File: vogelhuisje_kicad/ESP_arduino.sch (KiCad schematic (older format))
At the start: 6 parts, among them J5 PMS5003

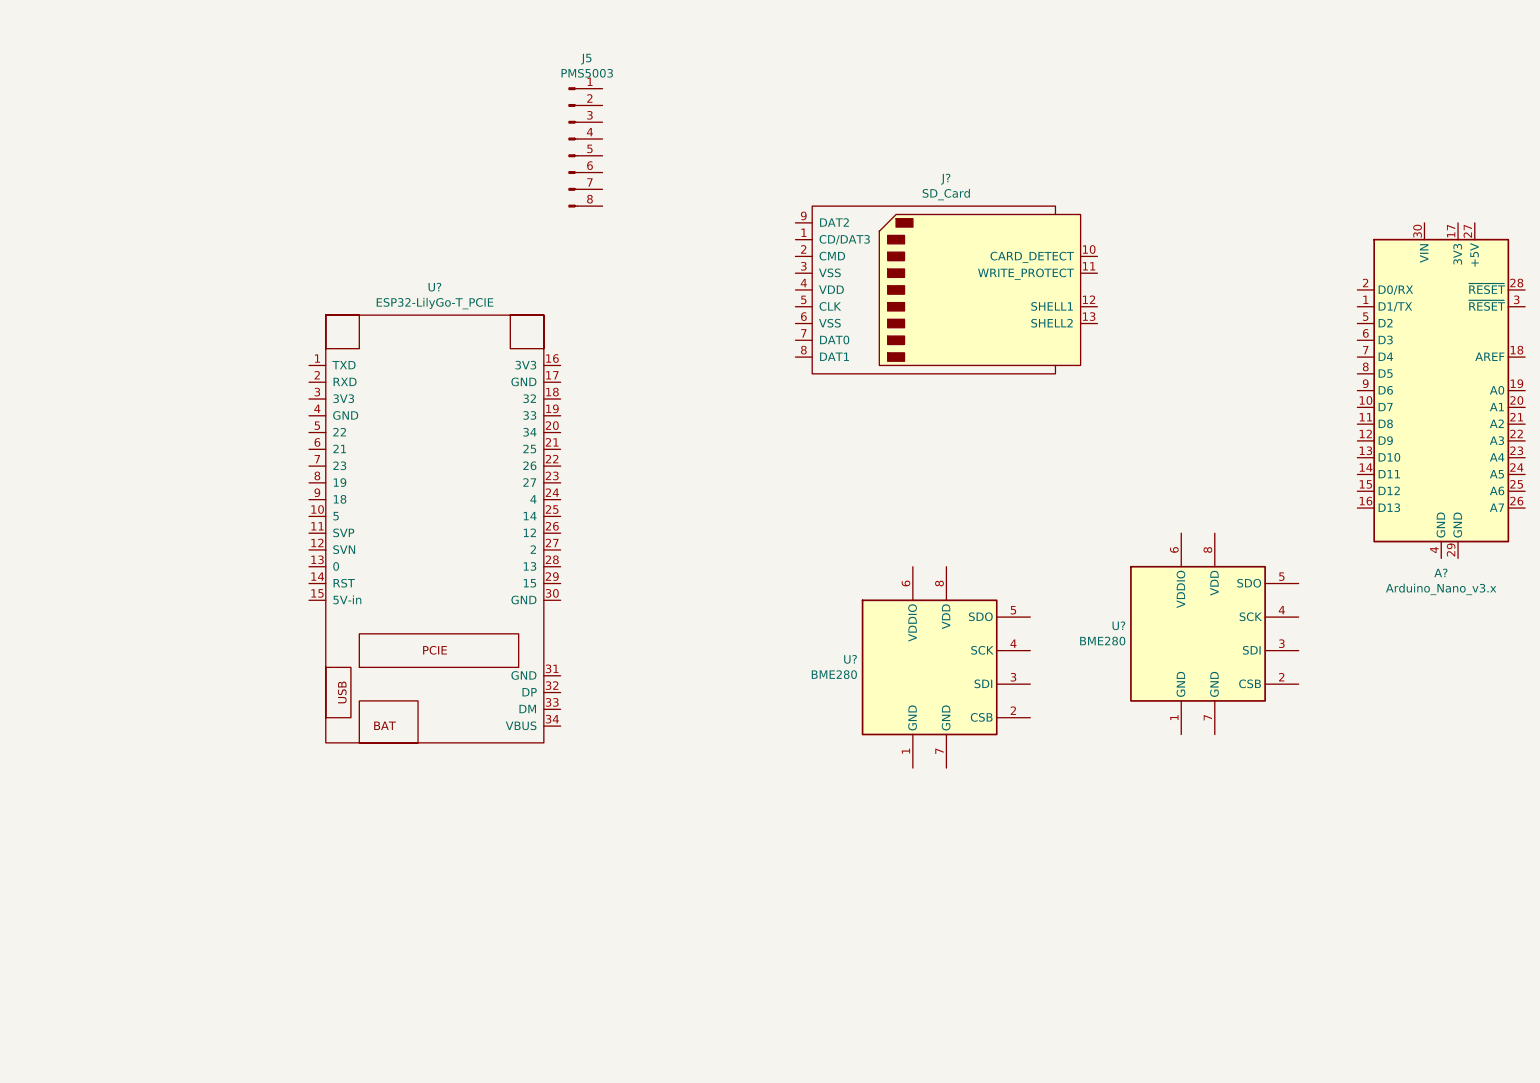
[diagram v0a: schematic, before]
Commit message: Add Camera to schematic
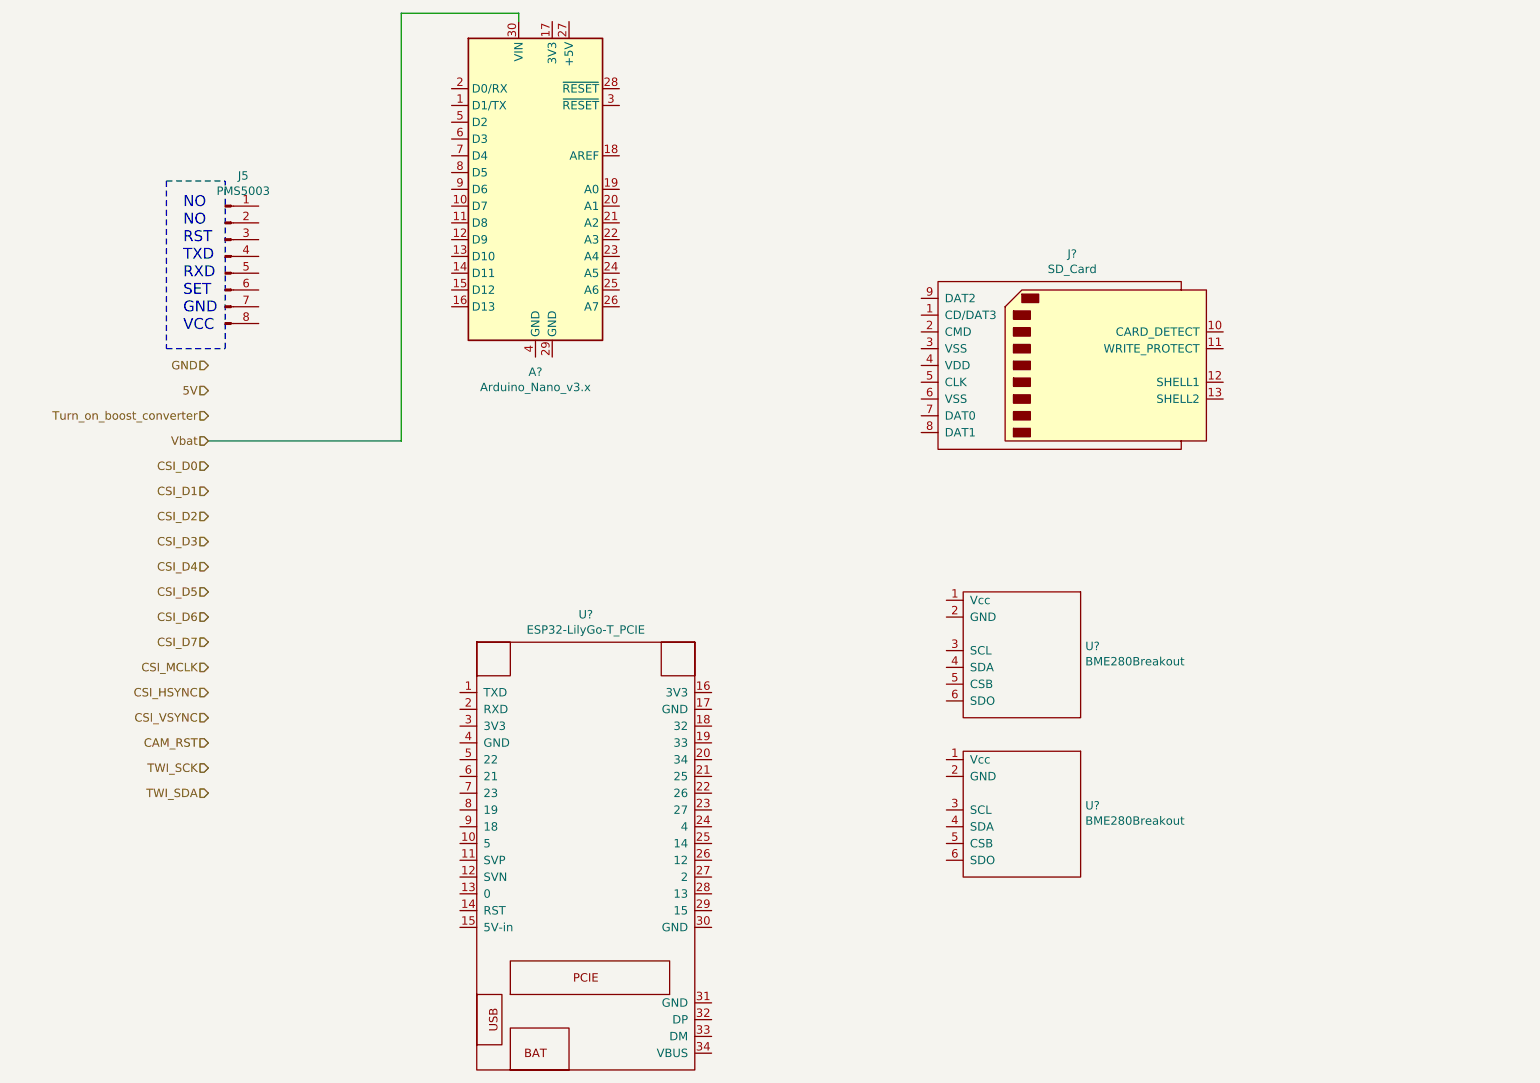
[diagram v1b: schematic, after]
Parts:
- removed U? (x2): BME280, Package_LGA:Bosch_LGA-8_2.5x2.5mm_P0.65mm_ClockwisePinNumbering, symbol Sensor:BME280
- added U? (x2): BME280Breakout, Components:Breakout-6, symbol voglehuisje_sensors_and_ESP:BME280Breakout
- J5: footprint (none) -> Components:PinHeader_1x08_P2.54mm_Vertical_G7
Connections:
- net Vbat: now reaches A?.30 (VIN)
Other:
- note added: "NO\nNO\nRST\nTXD\nRXD\nSET\nGND\nVCC"
- moved on the sheet: A?, J5, J?, U?
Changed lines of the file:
@@
 $Descr A4 11693 8268
 encoding utf-8
-Sheet 3 3
+Sheet 3 4
 Title ""
 Date ""
@@
 L MCU_Module:Arduino_Nano_v3.x A?
 U 1 1 6264AB53
-P 9350 2850
-F 0 "A?" H 9350 1761 50  0000 C CNN
-F 1 "Arduino_Nano_v3.x" H 9350 1670 50  0000 C CNN
-F 2 "Module:Arduino_Nano" H 9350 2850 50  0001 C CIN
-F 3 "http://www.mouser.com/pdfdocs/Gravitech_Arduino_Nano3_0.pdf" H 9350 2850 50  0001 C CNN
-	1    9350 2850
+P 3950 1650
+F 0 "A?" H 3950 561 50  0000 C CNN
+F 1 "Arduino_Nano_v3.x" H 3950 470 50  0000 C CNN
+F 2 "Module:Arduino_Nano" H 3950 1650 50  0001 C CIN
+F 3 "http://www.mouser.com/pdfdocs/Gravitech_Arduino_Nano3_0.pdf" H 3950 1650 50  0001 C CNN
+	1    3950 1650
 	1    0    0    -1
 $EndComp
@@
 L voglehuisje_sensors_and_ESP:ESP32-LilyGo-T_PCIE U?
 U 1 1 6264F9C2
-P 3300 4050
-F 0 "U?" H 3350 5865 50  0000 C CNN
-F 1 "ESP32-LilyGo-T_PCIE" H 3350 5774 50  0000 C CNN
-F 2 "Components:Tity-LilyGo" H 3250 4150 50  0001 C CNN
-F 3 "" H 3250 4150 50  0001 C CNN
-	1    3300 4050
+P 4200 6000
+F 0 "U?" H 4250 7815 50  0000 C CNN
+F 1 "ESP32-LilyGo-T_PCIE" H 4250 7724 50  0000 C CNN
+F 2 "Components:Tity-LilyGo" H 4150 6100 50  0001 C CNN
+F 3 "" H 4150 6100 50  0001 C CNN
+	1    4200 6000
 	1    0    0    -1
 $EndComp
@@
 L Connector:SD_Card J?
 U 1 1 62653AAF
-P 6400 2250
-F 0 "J?" H 6400 2915 50  0000 C CNN
-F 1 "SD_Card" H 6400 2824 50  0000 C CNN
-F 2 "" H 6400 2250 50  0001 C CNN
-F 3 "http://portal.fciconnect.com/Comergent//fci/drawing/10067847.pdf" H 6400 2250 50  0001 C CNN
-	1    6400 2250
-	1    0    0    -1
-$EndComp
-$Comp
-L Sensor:BME280 U?
-U 1 1 62653FC9
-P 6300 4500
-F 0 "U?" H 5871 4546 50  0000 R CNN
-F 1 "BME280" H 5871 4455 50  0000 R CNN
-F 2 "Package_LGA:Bosch_LGA-8_2.5x2.5mm_P0.65mm_ClockwisePinNumbering" H 7800 4050 50  0001 C CNN
-F 3 "https://ae-bst.resource.bosch.com/media/_tech/media/datasheets/BST-BME280-DS002.pdf" H 6300 4300 50  0001 C CNN
-	1    6300 4500
-	1    0    0    -1
-$EndComp
-$Comp
-L Sensor:BME280 U?
-U 1 1 626542C0
-P 7900 4300
-F 0 "U?" H 7471 4346 50  0000 R CNN
-F 1 "BME280" H 7471 4255 50  0000 R CNN
-F 2 "Package_LGA:Bosch_LGA-8_2.5x2.5mm_P0.65mm_ClockwisePinNumbering" H 9400 3850 50  0001 C CNN
-F 3 "https://ae-bst.resource.bosch.com/media/_tech/media/datasheets/BST-BME280-DS002.pdf" H 7900 4100 50  0001 C CNN
-	1    7900 4300
+P 7150 2700
+F 0 "J?" H 7150 3365 50  0000 C CNN
+F 1 "SD_Card" H 7150 3274 50  0000 C CNN
+F 2 "" H 7150 2700 50  0001 C CNN
+F 3 "http://portal.fciconnect.com/Comergent//fci/drawing/10067847.pdf" H 7150 2700 50  0001 C CNN
+	1    7150 2700
 	1    0    0    -1
 $EndComp
@@
 L Connector:Conn_01x08_Male J5
 U 1 1 62654811
-P 4150 1350
-F 0 "J5" H 4258 1831 50  0000 C CNN
-F 1 "PMS5003" H 4258 1740 50  0000 C CNN
-F 2 "" H 4150 1350 50  0001 C CNN
-F 3 "~" H 4150 1350 50  0001 C CNN
-	1    4150 1350
+P 2100 2050
+F 0 "J5" H 2208 2531 50  0000 C CNN
+F 1 "PMS5003" H 2208 2440 50  0000 C CNN
+F 2 "Components:PinHeader_1x08_P2.54mm_Vertical_G7" H 2100 2050 50  0001 C CNN
+F 3 "~" H 2100 2050 50  0001 C CNN
+	1    2100 2050
 	1    0    0    -1
 $EndComp
+$Comp
+L voglehuisje_sensors_and_ESP:BME280Breakout U?
+U 1 1 62697B14
+P 6850 4450
+F 0 "U?" H 7228 4526 50  0000 L CNN
+F 1 "BME280Breakout" H 7228 4435 50  0000 L CNN
+F 2 "Components:Breakout-6" H 6850 4450 50  0001 C CNN
+F 3 "" H 6850 4450 50  0001 C CNN
+	1    6850 4450
+	1    0    0    -1
+$EndComp
+$Comp
+L voglehuisje_sensors_and_ESP:BME280Breakout U?
+U 1 1 626985F8
+P 6850 5400
+F 0 "U?" H 7228 5476 50  0000 L CNN
+F 1 "BME280Breakout" H 7228 5385 50  0000 L CNN
+F 2 "Components:Breakout-6" H 6850 5400 50  0001 C CNN
+F 3 "" H 6850 5400 50  0001 C CNN
+	1    6850 5400
+	1    0    0    -1
+$EndComp
+Wire Notes Line style solid rgb(194, 14, 12)
+	1750 1600 1750 2600
+Wire Notes Line style solid rgb(194, 14, 12)
+	1750 2600 2100 2600
+Wire Notes Line style solid rgb(194, 14, 12)
+	1750 1600 2100 1600
+Text Notes 1850 2500 0    65   ~ 0
+NO\nNO\nRST\nTXD\nRXD\nSET\nGND\nVCC
+Wire Notes Line style solid rgb(194, 14, 12)
+	2100 2600 2100 1600
+Text HLabel 2000 2700 0    50   Input ~ 0
+GND
+Text HLabel 2000 2850 0    50   Input ~ 0
+5V
+Text HLabel 2000 3300 0    50   Input ~ 0
+CSI_D0
+Text HLabel 2000 3450 0    50   Input ~ 0
+CSI_D1
+Text HLabel 2000 3600 0    50   Input ~ 0
+CSI_D2
+Text HLabel 2000 3750 0    50   Input ~ 0
+CSI_D3
+Text HLabel 2000 3900 0    50   Input ~ 0
+CSI_D4
+Text HLabel 2000 4050 0    50   Input ~ 0
+CSI_D5
+Text HLabel 2000 4200 0    50   Input ~ 0
+CSI_D6
+Text HLabel 2000 4350 0    50   Input ~ 0
+CSI_D7
+Text HLabel 2000 4500 0    50   Input ~ 0
+CSI_MCLK
+Text HLabel 2000 4650 0    50   Input ~ 0
+CSI_HSYNC
+Text HLabel 2000 4800 0    50   Input ~ 0
+CSI_VSYNC
+Text HLabel 2000 4950 0    50   Input ~ 0
+CAM_RST
+Text HLabel 2000 5100 0    50   Input ~ 0
+TWI_SCK
+Text HLabel 2000 5250 0    50   Input ~ 0
+TWI_SDA
+Text HLabel 2000 3150 0    50   Input ~ 0
+Vbat
+Wire Wire Line
+	2000 3150 3150 3150
+Wire Wire Line
+	3150 3150 3150 600
+Wire Wire Line
+	3150 600  3850 600
+Wire Wire Line
+	3850 600  3850 650
+Text HLabel 2000 3000 0    50   Input ~ 0
+Turn_on_boost_converter
 $EndSCHEMATC

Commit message: Update Camera_module.sch, Camera_module.sch-bak, and 5 more files...
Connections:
- net 5V: now also J5.8 (Pin_8)
- net GND: now also A?.29 (GND), A?.4 (GND), J5.7 (Pin_7), U?.17 (GND), U?.2 (GND), U?.2 (GND), U?.30 (GND), U?.4 (GND)
- net at U?.16 (3V3): now also U?.1 (Vcc), U?.1 (Vcc)
- net 3V3: now reaches U?.3 (3V3)
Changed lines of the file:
@@
 Text HLabel 2000 3000 0    50   Input ~ 0
 Turn_on_boost_converter
+Wire Wire Line
+	2000 2850 2450 2850
+Wire Wire Line
+	2450 2850 2450 2450
+Wire Wire Line
+	2450 2450 2300 2450
+Wire Wire Line
+	5000 4650 5250 4650
+Wire Wire Line
+	5250 4650 5250 4100
+Wire Wire Line
+	5250 4100 6400 4100
+Wire Wire Line
+	5250 5050 6400 5050
+Wire Wire Line
+	5250 4650 5250 5050
+Connection ~ 5250 4650
+Wire Wire Line
+	5000 4750 5300 4750
+Wire Wire Line
+	5300 4750 5300 4200
+Wire Wire Line
+	5300 4200 6400 4200
+Wire Wire Line
+	5300 4750 5300 5150
+Wire Wire Line
+	5300 5150 5750 5150
+Connection ~ 5300 4750
+Text HLabel 2000 5400 0    50   Input ~ 0
+V_LED_switch-
+Text HLabel 2000 5550 0    50   Input ~ 0
+3V3
+Wire Wire Line
+	2000 5550 2900 5550
+Wire Wire Line
+	2900 5550 2900 4850
+Wire Wire Line
+	2900 4850 3500 4850
+$Comp
+L power:GND #PWR?
+U 1 1 626CC30D
+P 5750 5200
+F 0 "#PWR?" H 5750 4950 50  0001 C CNN
+F 1 "GND" H 5755 5027 50  0000 C CNN
+F 2 "" H 5750 5200 50  0001 C CNN
+F 3 "" H 5750 5200 50  0001 C CNN
+	1    5750 5200
+	1    0    0    -1
+$EndComp
+Wire Wire Line
+	5750 5200 5750 5150
+Connection ~ 5750 5150
+Wire Wire Line
+	5750 5150 6400 5150
+$Comp
+L power:GND #PWR?
+U 1 1 626CD7FE
+P 5050 6100
+F 0 "#PWR?" H 5050 5850 50  0001 C CNN
+F 1 "GND" H 5055 5927 50  0000 C CNN
+F 2 "" H 5050 6100 50  0001 C CNN
+F 3 "" H 5050 6100 50  0001 C CNN
+	1    5050 6100
+	1    0    0    -1
+$EndComp
+$Comp
+L power:GND #PWR?
+U 1 1 626CD9FD
+P 3400 5000
+F 0 "#PWR?" H 3400 4750 50  0001 C CNN
+F 1 "GND" H 3405 4827 50  0000 C CNN
+F 2 "" H 3400 5000 50  0001 C CNN
+F 3 "" H 3400 5000 50  0001 C CNN
+	1    3400 5000
+	1    0    0    -1
+$EndComp
+Wire Wire Line
+	3400 5000 3400 4950
+Wire Wire Line
+	3400 4950 3500 4950
+Wire Wire Line
+	5050 6100 5050 6050
+Wire Wire Line
+	5050 6050 5000 6050
+$Comp
+L power:GND #PWR?
+U 1 1 626CF2C3
+P 2100 2750
+F 0 "#PWR?" H 2100 2500 50  0001 C CNN
+F 1 "GND" H 2105 2577 50  0000 C CNN
+F 2 "" H 2100 2750 50  0001 C CNN
+F 3 "" H 2100 2750 50  0001 C CNN
+	1    2100 2750
+	1    0    0    -1
+$EndComp
+Wire Wire Line
+	2100 2750 2100 2700
+Wire Wire Line
+	2100 2700 2000 2700
+Wire Wire Line
+	2300 2350 2400 2350
+Wire Wire Line
+	2400 2350 2400 2700
+Wire Wire Line
+	2400 2700 2100 2700
+Connection ~ 2100 2700
+$Comp
+L power:GND #PWR?
+U 1 1 626D00C2
+P 4050 2700
+F 0 "#PWR?" H 4050 2450 50  0001 C CNN
+F 1 "GND" H 4055 2527 50  0000 C CNN
+F 2 "" H 4050 2700 50  0001 C CNN
+F 3 "" H 4050 2700 50  0001 C CNN
+	1    4050 2700
+	1    0    0    -1
+$EndComp
+Wire Wire Line
+	4050 2700 4050 2650
+Wire Wire Line
+	3950 2650 4050 2650
+Connection ~ 4050 2650
 $EndSCHEMATC
